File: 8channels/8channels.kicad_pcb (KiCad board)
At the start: 4 copper layers, 46 x 64 mm, 17 parts, among them J1 Conn_01x18_Female, J2 Conn_01x18_Male, P1 PCIEX1_02X18, P2 PCIEX1_02X18, U1 SN74CB3Q3251PWR, U2 SN74CB3Q3251PWR, U3 SN74CB3Q3251PWR, U4 SN74CB3Q3251PWR, U5 SN74CB3Q3251PWR

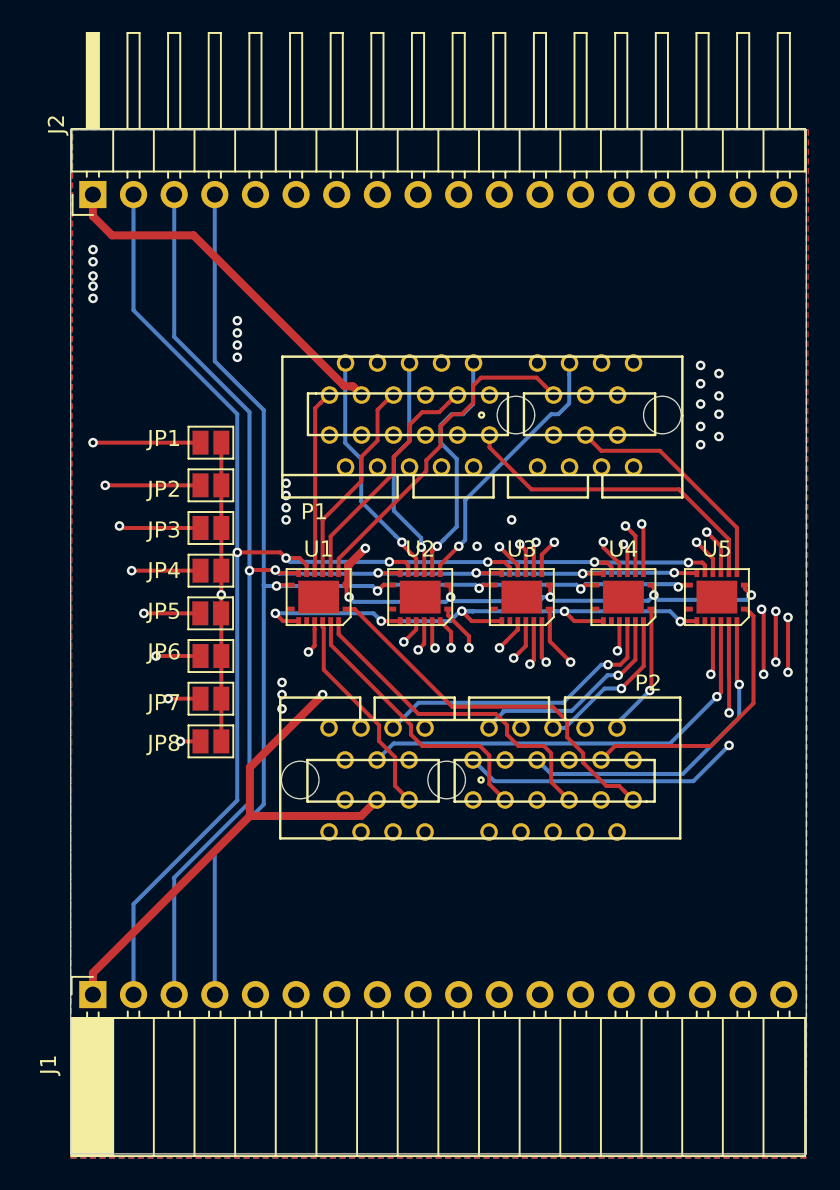
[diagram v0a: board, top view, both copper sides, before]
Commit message: Add caps & get rid of the jumpers & add two more GND lanes to the connector & remove two OE select signals
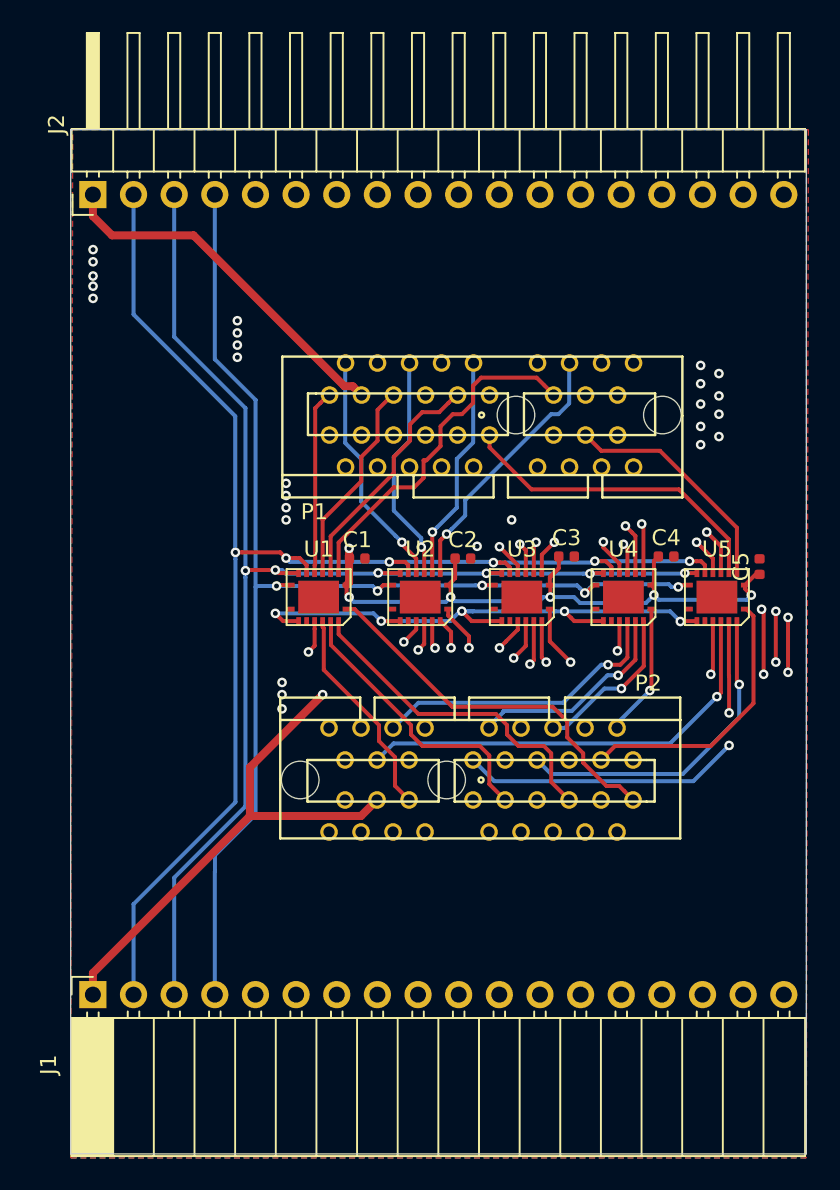
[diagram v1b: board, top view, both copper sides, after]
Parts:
- removed JP1, JP2, JP3, JP4, JP5, JP6, JP7, JP8: Jumper_NO_Small, Jumper:SolderJumper-2_P1.3mm_Open_Pad1.0x1.5mm
- added C1: C_Small, Capacitor_SMD:C_0402_1005Metric, F.Cu at (96.5, 102.7)
- added C2: C_Small, Capacitor_SMD:C_0402_1005Metric, F.Cu at (103.1, 102.7)
- added C3: C_Small, Capacitor_SMD:C_0402_1005Metric, F.Cu at (109.6, 102.6)
- added C4: C_Small, Capacitor_SMD:C_0402_1005Metric, F.Cu at (115.8, 102.6)
- added C5: C_Small, Capacitor_SMD:C_0402_1005Metric, F.Cu at (121.7, 103.3)
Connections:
- J1 pad 10: /OE6 -> (no net)
- J1 pad 11: /OE7 -> /GND
- J1 pad 12: /OE8 -> /GND
- J1 pad 5: /OE1 -> /OE2
- J1 pad 6: /OE2 -> /OE3
- J1 pad 7: /OE3 -> /OE4
- J1 pad 8: /OE4 -> /OE5
- J1 pad 9: /OE5 -> /OE6
- J2 pad 11: /OE7 -> /GND
- J2 pad 12: /OE8 -> /GND
- J2 pad 5: /OE1 -> /OE
- P1 pad A17: Net-(P1-PadA17) -> (no net)
- P1 pad A18: Net-(P1-PadA18) -> (no net)
- P1 pad B12: Net-(P1-PadB12) -> (no net)
- P1 pad B16: Net-(P1-PadB16) -> (no net)
- P1 pad B17: Net-(P1-PadB17) -> (no net)
- P1 pad B18: Net-(P1-PadB18) -> (no net)
- P1 pad B4: Net-(P1-PadB4) -> (no net)
- P1 pad B8: Net-(P1-PadB8) -> (no net)
- P2 pad A17: Net-(P2-PadA17) -> (no net)
- P2 pad A18: Net-(P2-PadA18) -> (no net)
- P2 pad B12: Net-(P2-PadB12) -> (no net)
- P2 pad B16: Net-(P2-PadB16) -> (no net)
- P2 pad B17: Net-(P2-PadB17) -> (no net)
- P2 pad B18: Net-(P2-PadB18) -> (no net)
- P2 pad B4: Net-(P2-PadB4) -> (no net)
- P2 pad B8: Net-(P2-PadB8) -> (no net)
- U1 pad 6: Net-(U1-Pad6) -> (no net)
- U2 pad 6: Net-(U2-Pad6) -> (no net)
- U3 pad 6: Net-(U3-Pad6) -> (no net)
- U4 pad 6: Net-(U4-Pad6) -> (no net)
- U5 pad 6: Net-(U5-Pad6) -> (no net)
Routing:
- net /OE8: track 83.9 -> 0.00 mm, vias 1 -> 0
- net /OE7: track 80.6 -> 0.00 mm, vias 1 -> 0
- net /OE1: track 67.2 -> 0.00 mm, vias 1 -> 0
- net /OE2: track 70.0 -> 54.5 mm, vias 1 -> 0
- net /OE3: track 72.6 -> 58.0 mm, vias 1 -> 0
- net /OE4: track 75.5 -> 62.0 mm, vias 1 -> 0
- net /OE5: track 76.9 -> 66.0 mm, vias 1 -> 0
- net /OE6: track 78.9 -> 69.9 mm, vias 1 -> 0
- net /VCC: track 141.0 -> 147.6 mm
- net /OE: track 58.6 -> 62.8 mm, vias 6 -> 5
- net /TCK|SWDCLK_6: track 15.5 -> 14.2 mm
- net /S1: track 87.8 -> 86.8 mm
- net /TMS|SWDIO_5: track 21.2 -> 22.0 mm

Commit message: Remade 8channel board
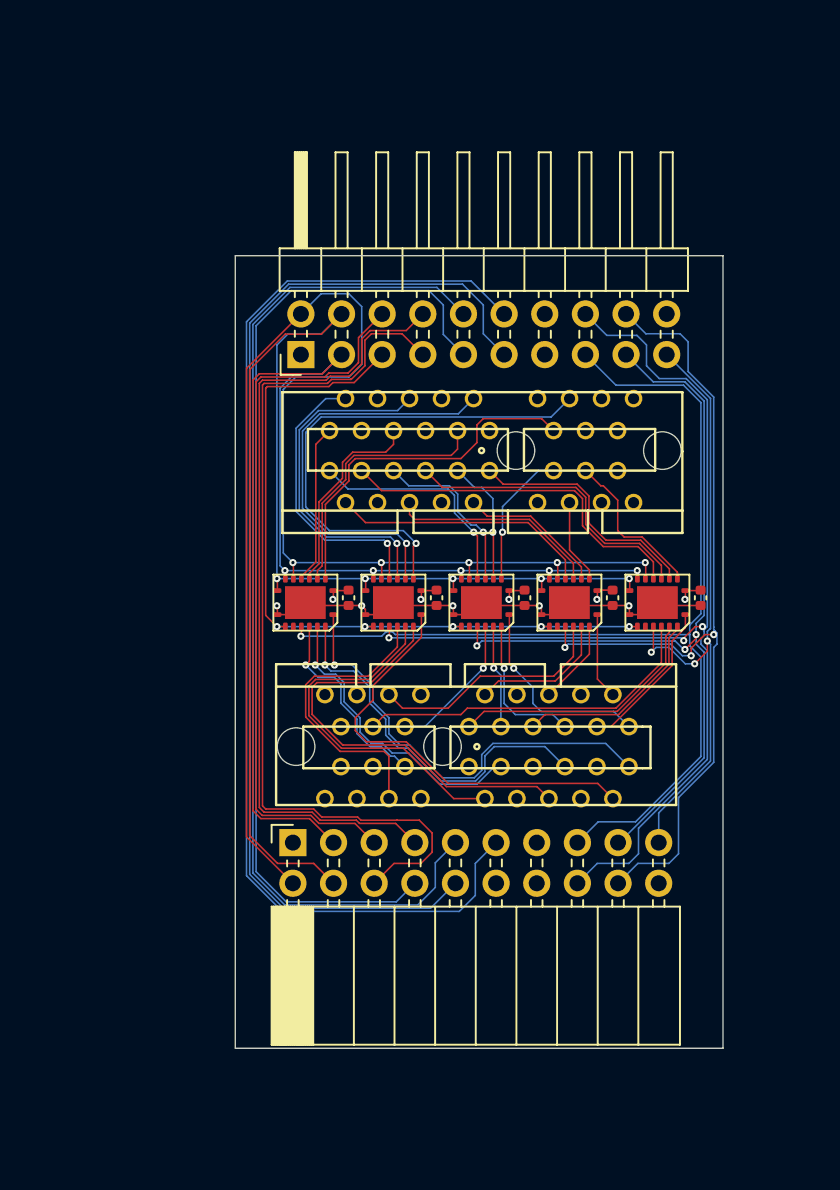
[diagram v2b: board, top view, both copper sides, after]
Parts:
- J1: footprint Connector_PinSocket_2.54mm:PinSocket_1x18_P2.54mm_Horizontal -> Connector_PinSocket_2.54mm:PinSocket_2x10_P2.54mm_Horizontal
- J2: footprint Connector_PinHeader_2.54mm:PinHeader_1x18_P2.54mm_Horizontal -> Connector_PinHeader_2.54mm:PinHeader_2x10_P2.54mm_Horizontal
- moved C5 25.8 mm to (96.0, 105.2), turned to 270 degrees
- moved C1 21.6 mm to (118.0, 105.2), turned to 270 degrees
- moved J2 16.4 mm to (93.0, 90.0)
- moved J1 15.7 mm to (92.5, 120.5)
- moved C4 14.6 mm to (101.5, 105.2), turned to 270 degrees
- moved C2 9.67 mm to (112.5, 105.2), turned to 270 degrees
- moved U5 3.73 mm to (115.3, 105.5)
- moved C3 3.68 mm to (107.0, 105.2), turned to 270 degrees
- moved U4 3.39 mm to (109.8, 105.5)
- moved U3 2.55 mm to (104.3, 105.5)
- moved P1 2.22 mm to (104.3, 96.0)
- moved P2 2.10 mm to (104.0, 114.5)
- moved U2 1.71 mm to (98.8, 105.5)
- moved U1 0.90 mm to (93.3, 105.5)
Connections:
- net /VCC renamed +3V3
- C1 pad 2: /GND -> GND
- C2 pad 2: /GND -> GND
- C3 pad 2: /GND -> GND
- C4 pad 2: /GND -> GND
- C5 pad 2: /GND -> GND
- J1 pad 10: (no net) -> /OE7
- J1 pad 11: /GND -> /OE8
- J1 pad 12: /GND -> Net-(J1-Pad12)
- J1 pad 13: /TMS|SWDIO -> GND
- J1 pad 14: /TCK|SWDCLK -> GND
- J1 pad 15: /TDO|SWO -> /TMS|SWDIO
- J1 pad 16: /TDI|EXT -> /TCK|SWDCLK
- J1 pad 17: /RST -> /TDO|SWO
- J1 pad 18: /GND -> /TDI|EXT
- J2 pad 11: /GND -> /OE7
- J2 pad 12: /GND -> /OE8
- J2 pad 13: /TMS|SWDIO -> GND
- J2 pad 14: /TCK|SWDCLK -> GND
- J2 pad 15: /TDO|SWO -> /TMS|SWDIO
- J2 pad 16: /TDI|EXT -> /TCK|SWDCLK
- J2 pad 17: /RST -> /TDO|SWO
- J2 pad 18: /GND -> /TDI|EXT
- P1 pad A12: /GND -> GND
- P1 pad A16: /GND -> GND
- P1 pad A17: (no net) -> Net-(P1-PadA17)
- P1 pad A18: (no net) -> Net-(P1-PadA18)
- P1 pad A4: /GND -> GND
- P1 pad A8: /GND -> GND
- P1 pad B12: (no net) -> Net-(P1-PadB12)
- P1 pad B16: (no net) -> Net-(P1-PadB16)
- P1 pad B17: (no net) -> Net-(P1-PadB17)
- P1 pad B18: (no net) -> Net-(P1-PadB18)
- P1 pad B4: (no net) -> Net-(P1-PadB4)
- P1 pad B8: (no net) -> Net-(P1-PadB8)
- P2 pad A12: /GND -> GND
- P2 pad A16: /GND -> GND
- P2 pad A17: (no net) -> Net-(P2-PadA17)
- P2 pad A18: (no net) -> Net-(P2-PadA18)
- P2 pad A4: /GND -> GND
- P2 pad A8: /GND -> GND
- P2 pad B12: (no net) -> Net-(P2-PadB12)
- P2 pad B16: (no net) -> Net-(P2-PadB16)
- P2 pad B17: (no net) -> Net-(P2-PadB17)
- P2 pad B18: (no net) -> Net-(P2-PadB18)
- P2 pad B4: (no net) -> Net-(P2-PadB4)
- P2 pad B8: (no net) -> Net-(P2-PadB8)
- U1 pad 0: (no net) -> GND
- U1 pad 6: (no net) -> Net-(U1-Pad6)
- U1 pad 8: /GND -> GND
- U2 pad 0: (no net) -> GND
- U2 pad 6: (no net) -> Net-(U2-Pad6)
- U2 pad 8: /GND -> GND
- U3 pad 0: (no net) -> GND
- U3 pad 6: (no net) -> Net-(U3-Pad6)
- U3 pad 8: /GND -> GND
- U4 pad 0: (no net) -> GND
- U4 pad 6: (no net) -> Net-(U4-Pad6)
- U4 pad 8: /GND -> GND
- U5 pad 0: (no net) -> GND
- U5 pad 6: (no net) -> Net-(U5-Pad6)
- U5 pad 8: /GND -> GND
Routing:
- net +3V3: track 147.6 -> 7.62 mm, vias 7 -> 5
- net /OE8: track 0.00 -> 72.1 mm
- net /OE7: track 0.00 -> 68.6 mm
- net GND: track 0.00 -> 30.9 mm, vias 0 -> 5
- net /TDO|SWO: track 77.6 -> 52.1 mm
- net /TMS|SWDIO: track 91.0 -> 66.2 mm, vias 3 -> 1
- net /TCK|SWDCLK: track 83.9 -> 66.9 mm
- net /TCK|SWDCLK_5: track 16.8 -> 32.1 mm
- net /RST: track 55.1 -> 39.8 mm, vias 1 -> 3
- net /OE: track 62.8 -> 48.0 mm
- net /TDI|EXT: track 68.7 -> 54.9 mm, vias 1 -> 3
- net /OE4: track 62.0 -> 50.1 mm
- net /TCK|SWDCLK_6: track 14.2 -> 26.0 mm
- net /TCK|SWDCLK_3: track 16.6 -> 27.1 mm, vias 1 -> 0
- net /OE2: track 54.5 -> 45.5 mm
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- added copper zone on In1.Cu, net +3V3
- added copper zone on In2.Cu, net GND
- removed copper zone on B.Cu, net /GND
- removed copper zone on F.Cu, net /GND
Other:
- board size 46 x 64 mm -> 30.5 x 49.5 mm
- net class Default: clearance 0.2 -> 0.1; trace_width 0.25 -> 0.1; via_dia 0.8 -> 0.45; via_drill 0.4 -> 0.2
- rule trace_clearance: 0.2 -> 0.1
- rule trace_min: 0.2 -> 0.1

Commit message: Fixes
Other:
- board text added: "Probe-rs Hive - 8 channels Design by Noah Huesser (@yatekii) Routing by Emil Fresk (@korken89)"

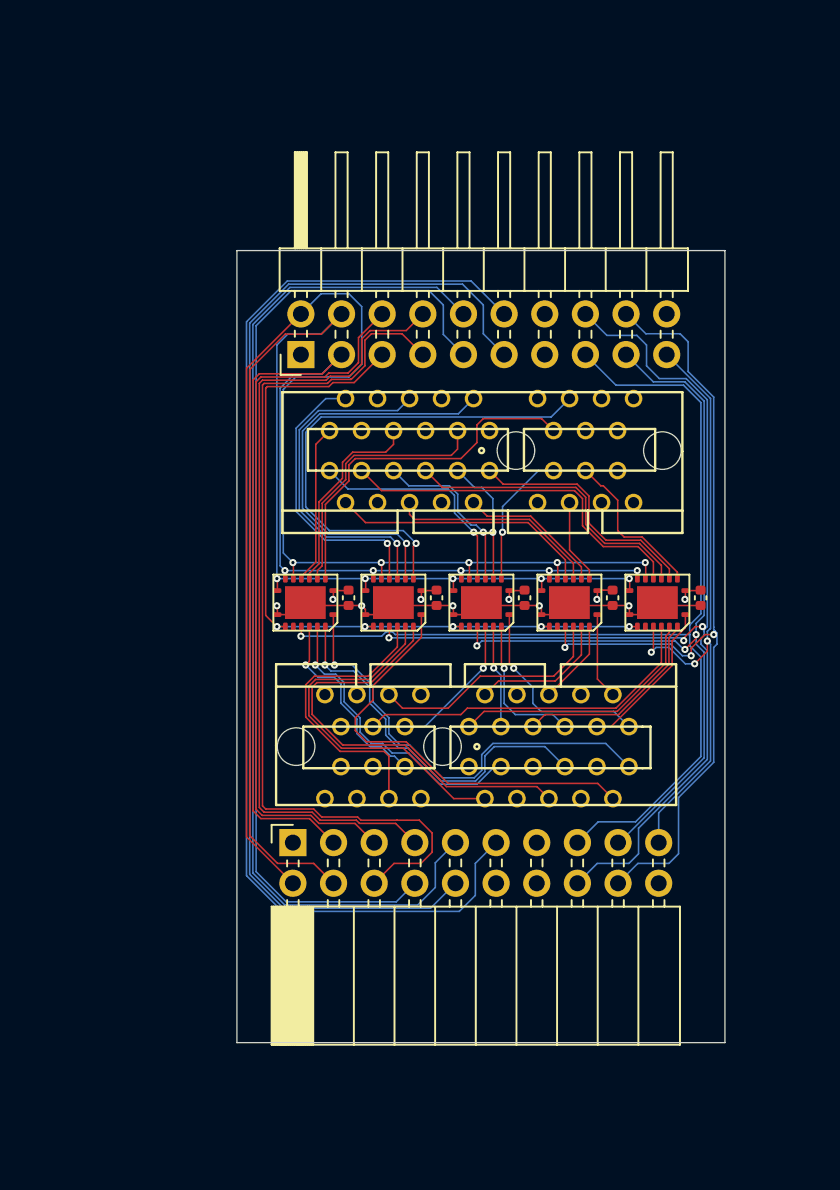
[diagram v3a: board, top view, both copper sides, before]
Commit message: Now with LDO per 8 channel board
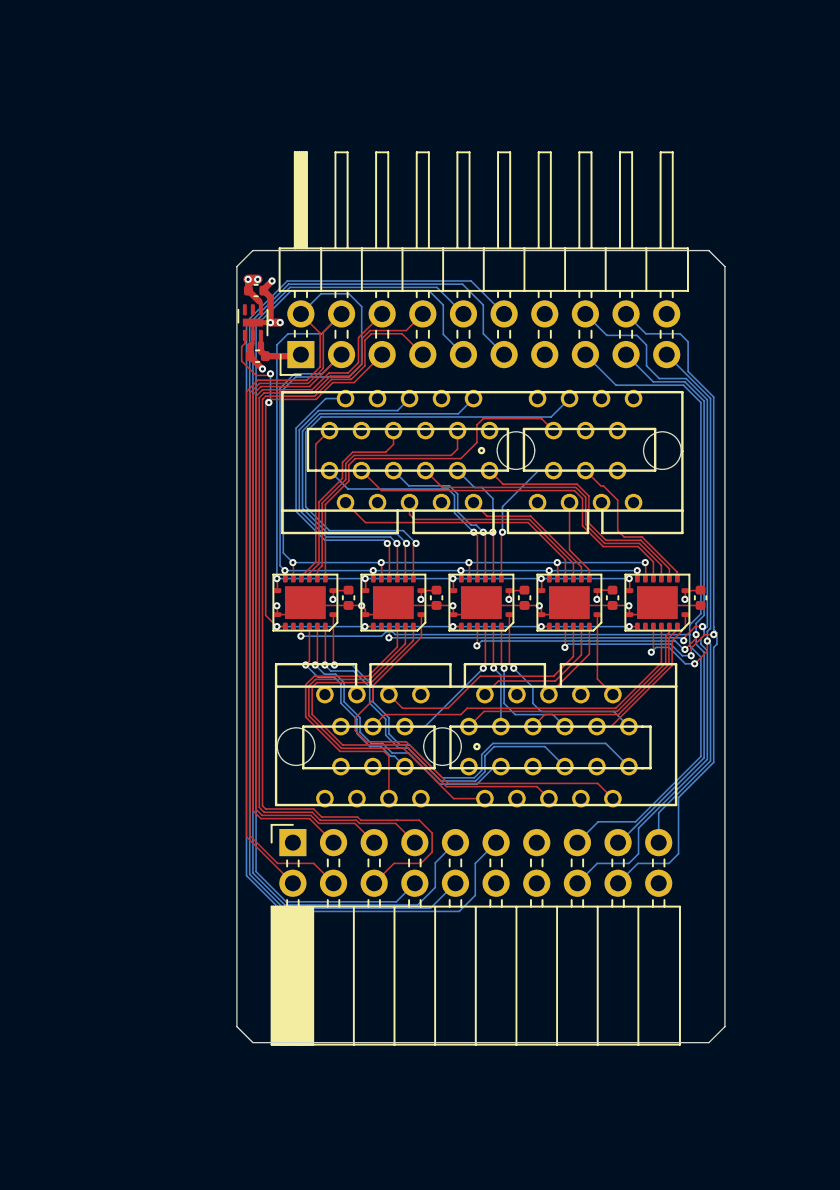
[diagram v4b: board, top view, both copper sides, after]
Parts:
- added C101: 1u, Capacitor_SMD:C_0402_1005Metric, F.Cu at (90.3, 90.1)
- added C102: 1u, Capacitor_SMD:C_0402_1005Metric, F.Cu at (90.2, 86.0)
- added U101: MIC5353-3.3YMT, Package_DFN_QFN:MLF-6-1EP_1.6x1.6mm_P0.5mm_EP0.5x1.26mm, F.Cu at (90.0, 88.0)
- C1, C2, C3, C4, C5: value C_Small -> 0.1u
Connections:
- J1 pad 1: +3V3 -> +5V
- J2 pad 1: +3V3 -> +5V
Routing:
- net +5V: track 0.00 -> 36.4 mm
- net GND: track 30.9 -> 38.9 mm, vias 5 -> 9
- net /OE: track 48.0 -> 53.3 mm, vias 5 -> 7
- net +3V3: track 7.62 -> 11.3 mm, vias 5 -> 7
- net /S0: track 90.1 -> 92.9 mm
- net /OE4: track 50.1 -> 49.5 mm
- net /OE2: track 45.5 -> 45.0 mm
- net /S1: track 79.8 -> 79.3 mm
- net /OE3: track 56.0 -> 55.5 mm
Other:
- outline, holes or cut-outs redrawn

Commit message: Add OE pulldown
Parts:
- added R101: 10k, Resistor_SMD:R_0402_1005Metric, F.Cu at (91.6, 108.1)
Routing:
- net /OE: track 53.3 -> 54.4 mm
- net GND: track 38.9 -> 39.9 mm, vias 9 -> 10

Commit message: Silk fix
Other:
- board text added: "probe-rs Hive - 8 channels Design by Noah Huesser (@yatekii) Routing by Emil Fresk (@korken89)"
- board text removed: "Probe-rs Hive - 8 channels Design by Noah Huesser (@yatekii) Routing by Emil Fresk (@korken89)"
